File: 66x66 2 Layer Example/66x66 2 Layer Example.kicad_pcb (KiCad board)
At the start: 2 copper layers, 66 x 66 mm, 65 parts, among them J1 Conn_01x02, J2 Conn_01x02, J3 USB_C_Receptacle_USB2.0_14P, J4 Conn_01x03, J5 Conn_01x04, Q1 DMG2305UX-7, SW1 SW_SPST, SW2 Reset, U1 W25Q128JVPIQ TR, U2 Voltage Regulator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

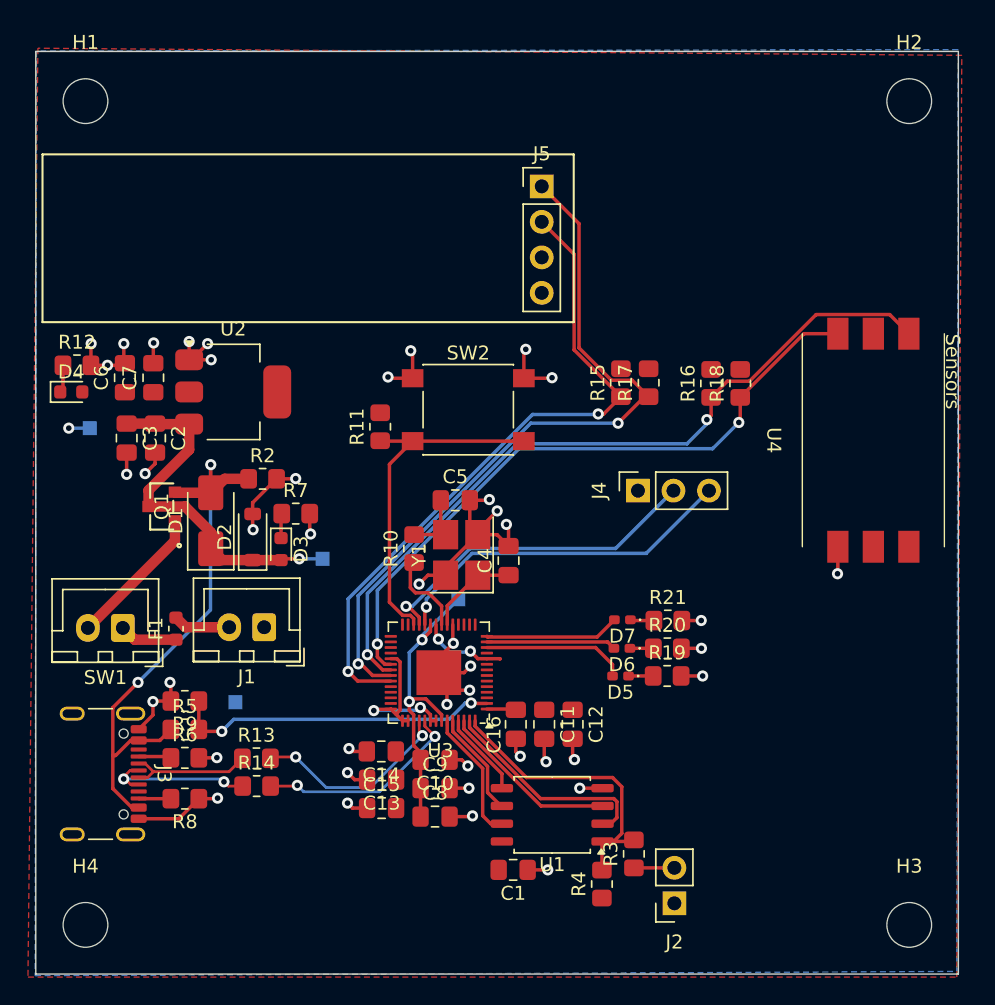
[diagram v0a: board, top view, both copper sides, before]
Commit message: Updated 66x66 to fix Clarence issues. Minimum 0.2mm
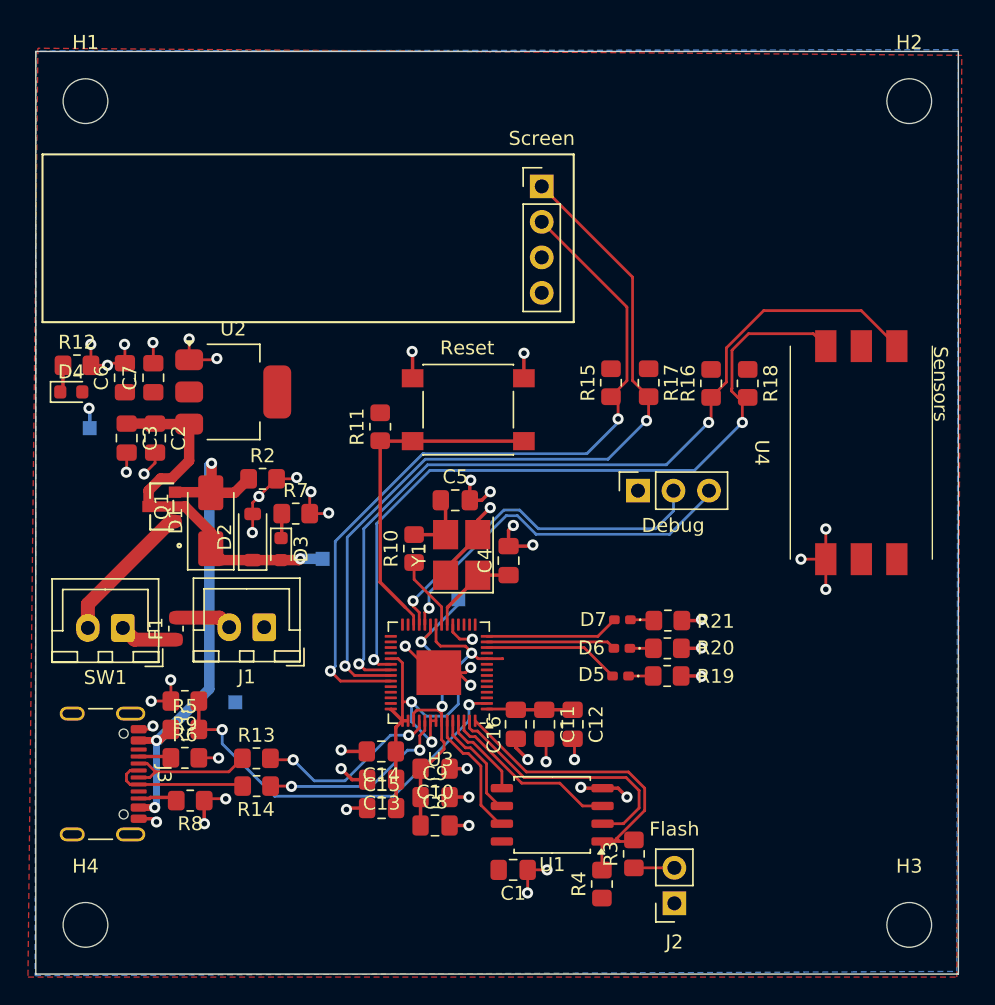
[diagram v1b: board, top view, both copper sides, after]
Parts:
- J2: value Conn_01x02 -> Flash
- J4: value Conn_01x03 -> Debug
- J5: value Conn_01x04 -> Screen
- moved U4 1.24 mm to (151.0, 86.5)
- moved R15 0.71 mm to (140.7, 81.5)
- moved C10 0.64 mm to (128.1, 109.1)
- moved C9 0.64 mm to (128.1, 111.1)
- moved C8 0.63 mm to (128.1, 113.2)
- moved R18 0.53 mm to (150.5, 81.5)
- moved R8 0.41 mm to (110.6, 111.4)
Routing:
- net +3V3: track 22.9 -> 41.4 mm, vias 5 -> 4
- net I2C0_SCL: track 48.9 -> 55.3 mm
- net I2C1_SDA: track 47.5 -> 53.6 mm
- net I2C1_SCL: track 55.0 -> 60.3 mm
- net GND: track 94.0 -> 88.9 mm, vias 43 -> 50
- net USB_DET: track 23.6 -> 28.6 mm
- net I2C0_SDA: track 53.3 -> 57.7 mm
- net VBUS: track 41.1 -> 37.8 mm, vias 2 -> 3
- net /QSPI_SD1: track 15.6 -> 18.8 mm
- net /QSPI_SS: track 22.0 -> 24.1 mm
- net D+: track 11.5 -> 9.76 mm, vias 2 -> 0
- net /SWD: track 24.4 -> 25.7 mm
- net /USB_D-: track 14.5 -> 13.3 mm
- net /SWCLK: track 25.3 -> 26.4 mm
- net /USB_D+: track 15.0 -> 14.0 mm
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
